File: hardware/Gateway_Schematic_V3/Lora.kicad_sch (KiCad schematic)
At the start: 4 parts, among them U12 Ipex, U8 SX1278 Lora Ra-02

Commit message: Update PCB Layout for Gateway (24/3/2026)
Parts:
- added CS1, GND1, MISO1, MOSI1, SCK1: TestPoint, IVS_NEW_FOOTPRINT:TestPoint_throughtHole_D1.0mm, symbol Connector:TestPoint
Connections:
- net GND: now also GND1.1
- net LORA.CS: now also CS1.1
- net LORA.MISO: now also MISO1.1
- net LORA.MOSI: now also MOSI1.1
- net LORA.SCK: now also SCK1.1

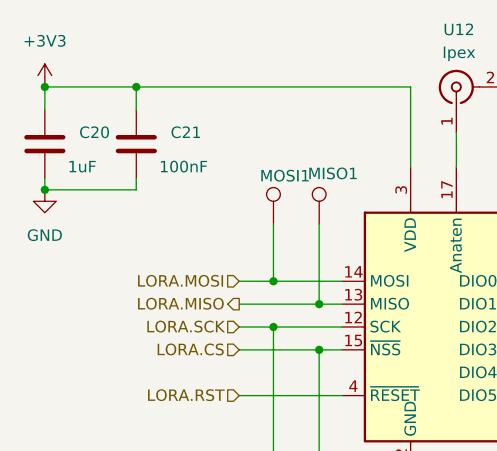
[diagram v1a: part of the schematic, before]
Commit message: Update PCB Layout after review 27/3/2026
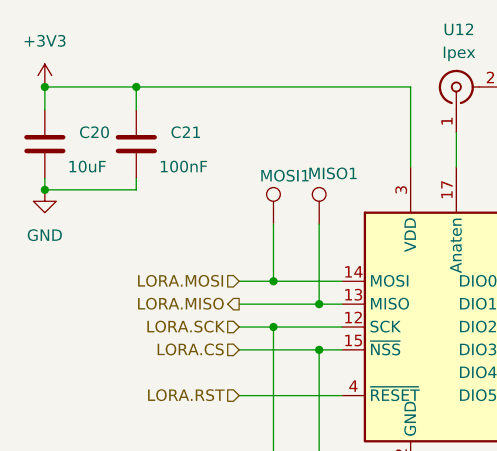
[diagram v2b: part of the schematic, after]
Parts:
- C20: value 1uF -> 10uF
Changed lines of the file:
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@@
 			)
 		)
-		(property "Value" "1uF"
+		(property "Value" "10uF"
 			(at 107.95 72.39 0)
 			(effects
